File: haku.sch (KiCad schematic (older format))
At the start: 125 parts

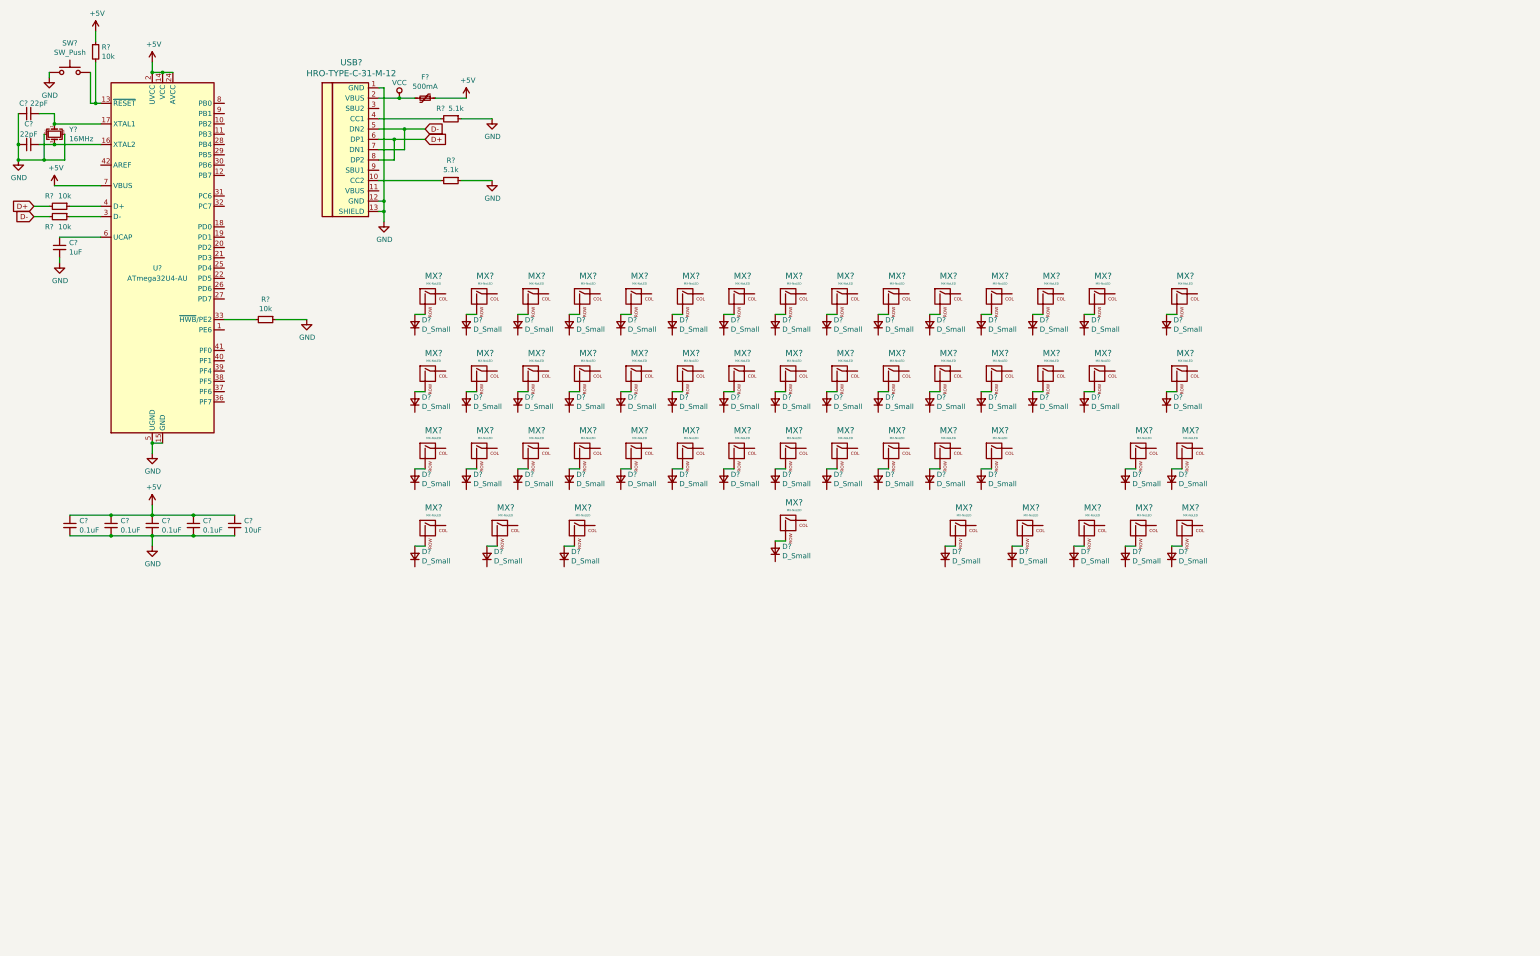
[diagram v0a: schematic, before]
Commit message: complete indicator leds, underglow, switch matrix, ESD
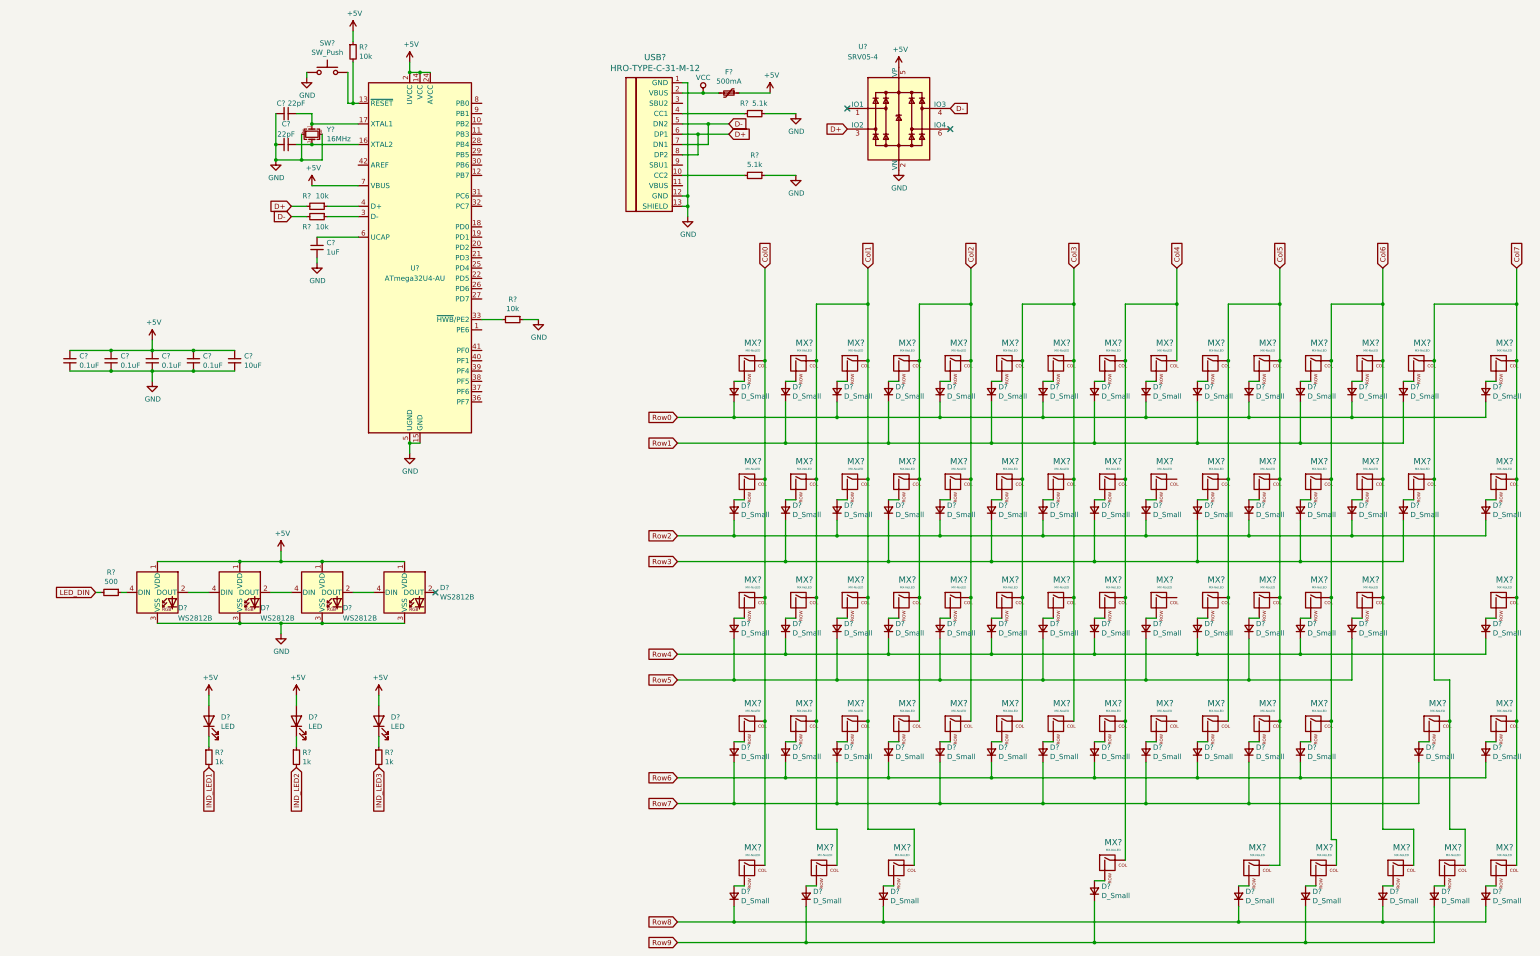
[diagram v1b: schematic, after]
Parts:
- added D? (x4): WS2812B, LED_SMD:LED_WS2812B_PLCC4_5.0x5.0mm_P3.2mm, symbol LED:WS2812B
- added D? (x3): LED, symbol Device:LED
- added D? (x14): D_Small, symbol Device:D_Small
- added MX? (x14): MX-NoLED, symbol MX_Alps_Hybrid:MX-NoLED
- added R?: 500, symbol Device:R_Small
- added R? (x3): 1k, symbol Device:R_Small
- added U?: SRV05-4, Package_TO_SOT_SMD:SOT-23-6, symbol Power_Protection:SRV05-4
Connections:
- net +5V: now also D?.1 (VDD), D?.1 (VDD), D?.1 (VDD), D?.1 (VDD), D?.2 (A), D?.2 (A), D?.2 (A), U?.5 (VP)
- net D+: now also U?.3 (IO2)
- net D-: now also U?.4 (IO3)
- net GND: now also D?.3 (VSS), D?.3 (VSS), D?.3 (VSS), D?.3 (VSS), U?.2 (VN)
- net Col0: now reaches MX?.1 (COL)
- net Col0: now also MX?.1 (COL), MX?.1 (COL), MX?.1 (COL), MX?.1 (COL)
- net Row0: now reaches D?.1 (K)
- net Row0: now also D?.1 (K), D?.1 (K), D?.1 (K), D?.1 (K), D?.1 (K), D?.1 (K), D?.1 (K)
- net Col1: now reaches MX?.1 (COL)
- net Col1: now also MX?.1 (COL), MX?.1 (COL), MX?.1 (COL), MX?.1 (COL), MX?.1 (COL), MX?.1 (COL), MX?.1 (COL), MX?.1 (COL), MX?.1 (COL)
- net Row1: now reaches D?.1 (K)
- net Row1: now also D?.1 (K), D?.1 (K), D?.1 (K), D?.1 (K), D?.1 (K), D?.1 (K)
- net Col2: now reaches MX?.1 (COL)
- net Col2: now also MX?.1 (COL), MX?.1 (COL), MX?.1 (COL), MX?.1 (COL), MX?.1 (COL), MX?.1 (COL), MX?.1 (COL)
- net Col3: now reaches MX?.1 (COL)
- net Col3: now also MX?.1 (COL), MX?.1 (COL), MX?.1 (COL), MX?.1 (COL), MX?.1 (COL), MX?.1 (COL), MX?.1 (COL)
- net Col4: now reaches MX?.1 (COL)
- net Col4: now also MX?.1 (COL), MX?.1 (COL), MX?.1 (COL), MX?.1 (COL), MX?.1 (COL)
- net Col5: now reaches MX?.1 (COL)
- net Col5: now also MX?.1 (COL), MX?.1 (COL), MX?.1 (COL), MX?.1 (COL), MX?.1 (COL), MX?.1 (COL), MX?.1 (COL), MX?.1 (COL)
- net Col6: now reaches MX?.1 (COL)
- net Col6: now also MX?.1 (COL), MX?.1 (COL), MX?.1 (COL), MX?.1 (COL), MX?.1 (COL), MX?.1 (COL), MX?.1 (COL), MX?.1 (COL)
- net Col7: now reaches MX?.1 (COL)
- net Col7: now also MX?.1 (COL), MX?.1 (COL), MX?.1 (COL), MX?.1 (COL), MX?.1 (COL), MX?.1 (COL), MX?.1 (COL), MX?.1 (COL)
- net Row2: now reaches D?.1 (K)
- net Row2: now also D?.1 (K), D?.1 (K), D?.1 (K), D?.1 (K), D?.1 (K), D?.1 (K), D?.1 (K)
- net Row3: now reaches D?.1 (K)
- net Row3: now also D?.1 (K), D?.1 (K), D?.1 (K), D?.1 (K), D?.1 (K), D?.1 (K)
- net Row5: now reaches D?.1 (K)
- net Row5: now also D?.1 (K), D?.1 (K), D?.1 (K), D?.1 (K), D?.1 (K), D?.1 (K)
- net Row4: now reaches D?.1 (K)
- net Row4: now also D?.1 (K), D?.1 (K), D?.1 (K), D?.1 (K), D?.1 (K), D?.1 (K)
- net Row8: now reaches D?.1 (K)
- net Row8: now also D?.1 (K), D?.1 (K), D?.1 (K), D?.1 (K)
- net Row9: now reaches D?.1 (K)
- net Row9: now also D?.1 (K), D?.1 (K), D?.1 (K)
- new net: D?.2 (DOUT), D?.4 (DIN) (x3)
- new net: D?.4 (DIN), R?.1
- new net: D?.1 (K), R?.1 (x3)
- new net: D?.2 (A), MX?.2 (ROW) (x14)
- new net IND_LED1: R?.2
- new net IND_LED2: R?.2
- new net IND_LED3: R?.2
- new net LED_DIN: R?.2
- new net Row6: D?.1 (K), D?.1 (K), D?.1 (K), D?.1 (K), D?.1 (K), D?.1 (K), D?.1 (K)
- new net Row7: D?.1 (K), D?.1 (K), D?.1 (K), D?.1 (K), D?.1 (K), D?.1 (K), D?.1 (K)
- no-connect marks 0 -> 3
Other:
- moved on the sheet: C?, D?, F?, MX?, R?, SW?, U?, USB?, Y?

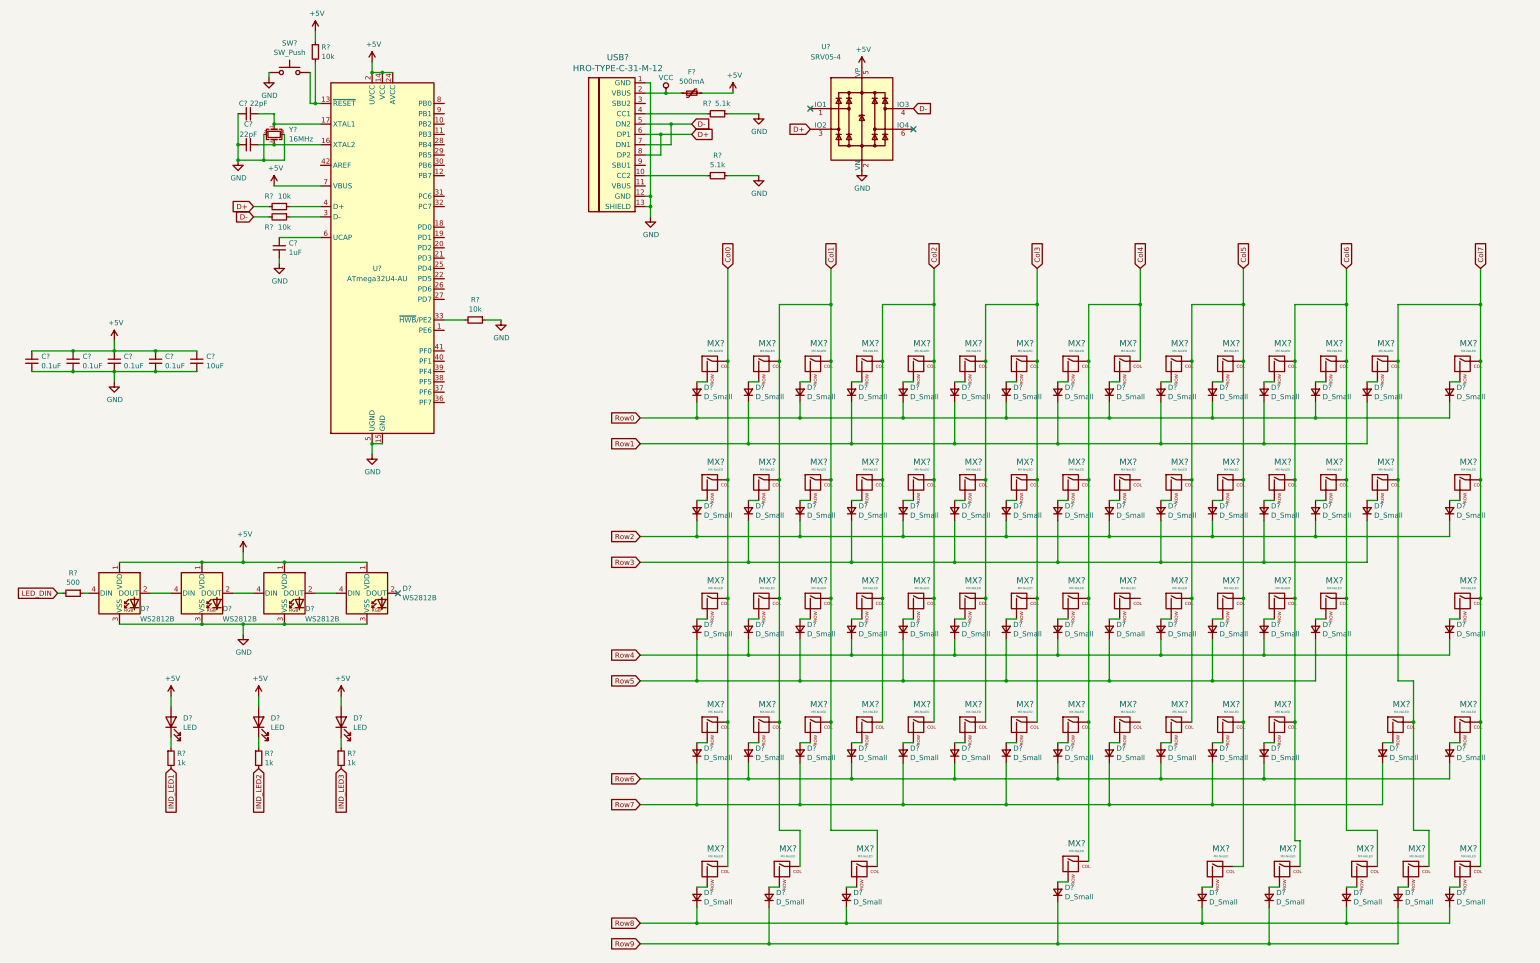
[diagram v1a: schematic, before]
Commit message: update switch matrix, assign footprints
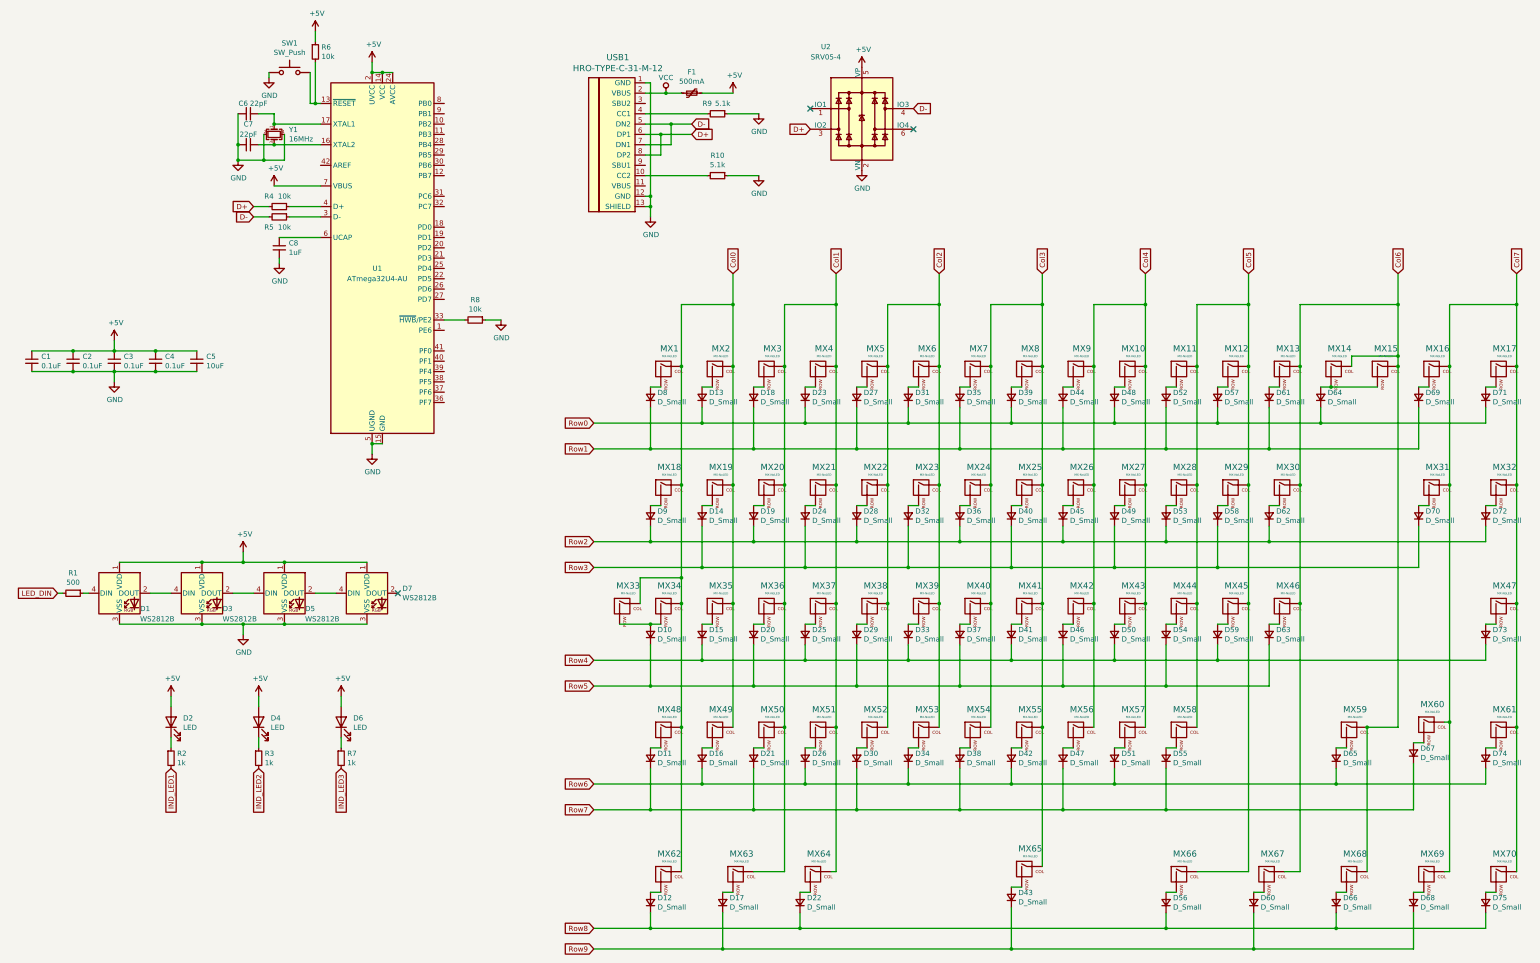
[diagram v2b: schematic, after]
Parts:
- added D69: D_Small, Diode_SMD:D_SOD-123, symbol Device:D_Small
- added MX15: MX-NoLED, MX_Only:MXOnly-2U-NoLED, symbol MX_Alps_Hybrid:MX-NoLED
- added MX16: MX-NoLED, MX_Only:MXOnly-1U-NoLED, symbol MX_Alps_Hybrid:MX-NoLED
- added MX33: MX-NoLED, MX_Only:MXOnly-1.25U-NoLED, symbol MX_Alps_Hybrid:MX-NoLED
- C1, C2, C3, C4, C5, C6, C7, C8: renamed from C?; footprint (none) -> Capacitor_SMD:C_0805_2012Metric
- D10, D11, D12, D13, D14, D15, D16, D17, D18, D19, D20, D21, D22, D23, D24, D25, D26, D27, D28, D29, D30, D31, D32, D33, D34, D35, D36, D37, D38, D39, D40, D41, D42, D43, D44, D45, D46, D47, D48, D49, D50, D51, D52, D53, D54, D55, D56, D57, D58, D59, D60, D61, D62, D63, D64, D65, D66, D67, D68, D70, D71, D72, D73, D74, D75, D8, D9: renamed from D?; footprint (none) -> Diode_SMD:D_SOD-123
- D2, D4, D6: renamed from D?; footprint (none) -> random-keyboard-parts:LED_D3.0mm-Pretty
- F1: renamed from F?; footprint (none) -> Fuse:Fuse_1206_3216Metric
- MX1, MX10, MX11, MX12, MX13, MX14, MX17, MX19, MX2, MX20, MX21, MX22, MX23, MX24, MX25, MX26, MX27, MX28, MX29, MX3, MX30, MX32, MX35, MX36, MX37, MX38, MX39, MX4, MX40, MX41, MX42, MX43, MX44, MX45, MX47, MX49, MX5, MX50, MX51, MX52, MX53, MX54, MX55, MX56, MX57, MX58, MX6, MX60, MX61, MX63, MX68, MX69, MX7, MX70, MX8, MX9: renamed from MX?; footprint (none) -> MX_Only:MXOnly-1U-NoLED
- MX18, MX31, MX62, MX64, MX66, MX67: renamed from MX?; footprint (none) -> MX_Only:MXOnly-1.5U-NoLED
- MX34: renamed from MX?; footprint (none) -> MX_Only:MXOnly-1.75U-NoLED
- MX46, MX48: renamed from MX?; footprint (none) -> MX_Only:MXOnly-2.25U-NoLED
- MX59: renamed from MX?; footprint (none) -> MX_Only:MXOnly-2.75U-NoLED
- MX65: renamed from MX?; footprint (none) -> MX_Only:MXOnly-7U-ReversedStabilizers-NoLED
- R1, R10, R2, R3, R4, R5, R6, R7, R8, R9: renamed from R?; footprint (none) -> Resistor_SMD:R_0805_2012Metric
- SW1: renamed from SW?; footprint (none) -> random-keyboard-parts:SKQG-1155865
- USB1: renamed from USB?; footprint (none) -> Type-C:HRO-TYPE-C-31-M-12-HandSoldering
- Y1: renamed from Y?; footprint (none) -> Crystal:Crystal_SMD_3225-4Pin_3.2x2.5mm
- gave numbers to parts that had none: 6
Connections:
- net Col0: now also MX19.1 (COL), MX2.1 (COL), MX35.1 (COL), MX49.1 (COL), MX33.1 (COL)
- net Col1: now also MX21.1 (COL), MX37.1 (COL), MX4.1 (COL), MX51.1 (COL); no longer MX19.1 (COL), MX2.1 (COL), MX35.1 (COL), MX49.1 (COL)
- net Col2: now also MX23.1 (COL), MX39.1 (COL), MX53.1 (COL), MX6.1 (COL); no longer MX21.1 (COL), MX37.1 (COL), MX4.1 (COL), MX51.1 (COL)
- net Col3: now also MX25.1 (COL), MX41.1 (COL), MX55.1 (COL), MX65.1 (COL), MX8.1 (COL); no longer MX23.1 (COL), MX39.1 (COL), MX53.1 (COL), MX6.1 (COL)
- net Col4: now also MX10.1 (COL), MX26.1 (COL), MX27.1 (COL), MX42.1 (COL), MX43.1 (COL), MX56.1 (COL), MX57.1 (COL); no longer MX25.1 (COL), MX41.1 (COL), MX55.1 (COL), MX65.1 (COL), MX8.1 (COL)
- net Col5: now also MX12.1 (COL), MX29.1 (COL), MX45.1 (COL); no longer MX10.1 (COL), MX27.1 (COL), MX43.1 (COL), MX57.1 (COL)
- net Col6: now also MX14.1 (COL), MX15.1 (COL); no longer MX12.1 (COL), MX29.1 (COL), MX45.1 (COL)
- net Col7: now also MX16.1 (COL); no longer MX14.1 (COL)
- net Row0: now also D13.1 (K), D23.1 (K), D31.1 (K), D39.1 (K), D48.1 (K), D57.1 (K), D64.1 (K); no longer D18.1 (K), D27.1 (K), D35.1 (K), D44.1 (K), D52.1 (K), D61.1 (K), D8.1 (K)
- net Row1: now also D18.1 (K), D27.1 (K), D35.1 (K), D44.1 (K), D52.1 (K), D61.1 (K), D8.1 (K), D69.1 (K); no longer D13.1 (K), D23.1 (K), D31.1 (K), D39.1 (K), D48.1 (K), D57.1 (K), D64.1 (K)
- net at D64.2 (A), MX14.2 (ROW): now also MX15.2 (ROW)
- net at D10.2 (A), MX34.2 (ROW): now also MX33.2 (ROW)
- new net: D69.2 (A), MX16.2 (ROW)
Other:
- moved on the sheet: D10, D11, D12, D13, D14, D15, D16, D17, D18, D19, D20, D21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

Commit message: place components on pcb
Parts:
- added D76, D77, D78: WS2812B, LED_SMD:LED_WS2812B_PLCC4_5.0x5.0mm_P3.2mm, symbol LED:WS2812B
- renumbered D3 to D2, D5 to D3, D7 to D4, D2 to D5, D4 to D6, D6 to D7
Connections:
- net +5V: now also D76.1 (VDD), D77.1 (VDD), D78.1 (VDD)
- net Col0: now also MX63.1 (COL)
- net Col1: no longer MX63.1 (COL)
- net GND: now also D76.3 (VSS), D77.3 (VSS), D78.3 (VSS)
- net at D4.2 (DOUT): now also D76.4 (DIN)
- new net: D76.2 (DOUT), D77.4 (DIN)
- new net: D77.2 (DOUT), D78.4 (DIN)
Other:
- moved on the sheet: D1, D2, D3, D4, D5, D6, D7, R1, R2, R3, R7

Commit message: begin routing
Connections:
- net D1-: now reaches R5.1, U1.3 (D-)
- net D1+: now reaches R4.1, U1.4 (D+)
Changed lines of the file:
@@
 Wire Wire Line
 	14500 9550 14500 9900
+Text Label 3750 2700 0    50   ~ 0
+D1+
+Text Label 3750 2800 0    50   ~ 0
+D1-
 $EndSCHEMATC

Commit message: complete routing
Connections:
- net Col0: now also U1.8 (PB0)
- net Col1: now also U1.11 (PB3)
- net Col2: now also U1.36 (PF7)
- net Col3: now also U1.39 (PF4)
- net Col4: now also U1.31 (PC6)
- net Col5: now also U1.38 (PF5)
- net Col6: now also U1.37 (PF6)
- net Col7: now also U1.32 (PC7)
- net IND_LED1: now also U1.27 (PD7)
- net IND_LED2: now also U1.28 (PB4)
- net IND_LED3: now also U1.1 (PE6)
- net LED_DIN: now also U1.18 (PD0)
- net Row0: now also U1.19 (PD1)
- net Row1: now also U1.20 (PD2)
- net Row2: now also U1.25 (PD4)
- net Row3: now also U1.26 (PD6)
- net Row4: now also U1.30 (PB6)
- net Row5: now also U1.29 (PB5)
- net Row6: now also U1.10 (PB2)
- net Row7: now also U1.9 (PB1)
- net Row8: now also U1.40 (PF1)
- net Row9: now also U1.41 (PF0)
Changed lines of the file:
@@
 Text Label 3750 2800 0    50   ~ 0
 D1-
+Text GLabel 5100 2900 2    50   Input ~ 0
+LED_DIN
+Text GLabel 5100 1700 2    50   Input ~ 0
+Col0
+Text GLabel 5100 2000 2    50   Input ~ 0
+Col1
+Text GLabel 5100 1900 2    50   Input ~ 0
+Row6
+Text GLabel 5100 1800 2    50   Input ~ 0
+Row7
+Text GLabel 5100 4300 2    50   Input ~ 0
+Col3
+Text GLabel 5100 4200 2    50   Input ~ 0
+Row8
+Text GLabel 5100 4100 2    50   Input ~ 0
+Row9
+Text GLabel 5100 4600 2    50   Input ~ 0
+Col2
+Text GLabel 5100 3000 2    50   Input ~ 0
+Row0
+Text GLabel 5100 3100 2    50   Input ~ 0
+Row1
+Text GLabel 5100 4500 2    50   Input ~ 0
+Col6
+Text GLabel 5100 2700 2    50   Input ~ 0
+Col7
+Text GLabel 5100 4400 2    50   Input ~ 0
+Col5
+Text GLabel 5100 2600 2    50   Input ~ 0
+Col4
+Text GLabel 5100 3300 2    50   Input ~ 0
+Row2
+Text GLabel 5100 3500 2    50   Input ~ 0
+Row3
+Text GLabel 5100 2300 2    50   Input ~ 0
+Row4
+Text GLabel 5100 2200 2    50   Input ~ 0
+Row5
+Text GLabel 5100 3900 2    50   Input ~ 0
+IND_LED3
+Text GLabel 5100 3600 2    50   Input ~ 0
+IND_LED1
+Text GLabel 5100 2100 2    50   Input ~ 0
+IND_LED2
 $EndSCHEMATC

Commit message: remove silkscreen artwork, add exposed soldermask artwork
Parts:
- R4, R5: value 10k -> 22
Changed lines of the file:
@@
 P 3500 2700
 F 0 "R4" V 3400 2600 50  0000 C CNN
-F 1 "10k" V 3400 2750 50  0000 C CNN
+F 1 "22" V 3400 2750 50  0000 C CNN
 F 2 "Resistor_SMD:R_0805_2012Metric" H 3500 2700 50  0001 C CNN
 F 3 "~" H 3500 2700 50  0001 C CNN
@@
 P 3500 2800
 F 0 "R5" V 3600 2700 50  0000 C CNN
-F 1 "10k" V 3600 2850 50  0000 C CNN
+F 1 "22" V 3600 2850 50  0000 C CNN
 F 2 "Resistor_SMD:R_0805_2012Metric" H 3500 2800 50  0001 C CNN
 F 3 "~" H 3500 2800 50  0001 C CNN
